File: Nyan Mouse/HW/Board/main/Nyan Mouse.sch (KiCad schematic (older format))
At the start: 11 parts, among them M101 BATTBALANCE-2S, P101 Controller Connector, P102 CONN_4, P103 CONN_2, P104 CONN_2, U101 DRV8837, U102 DRV8837

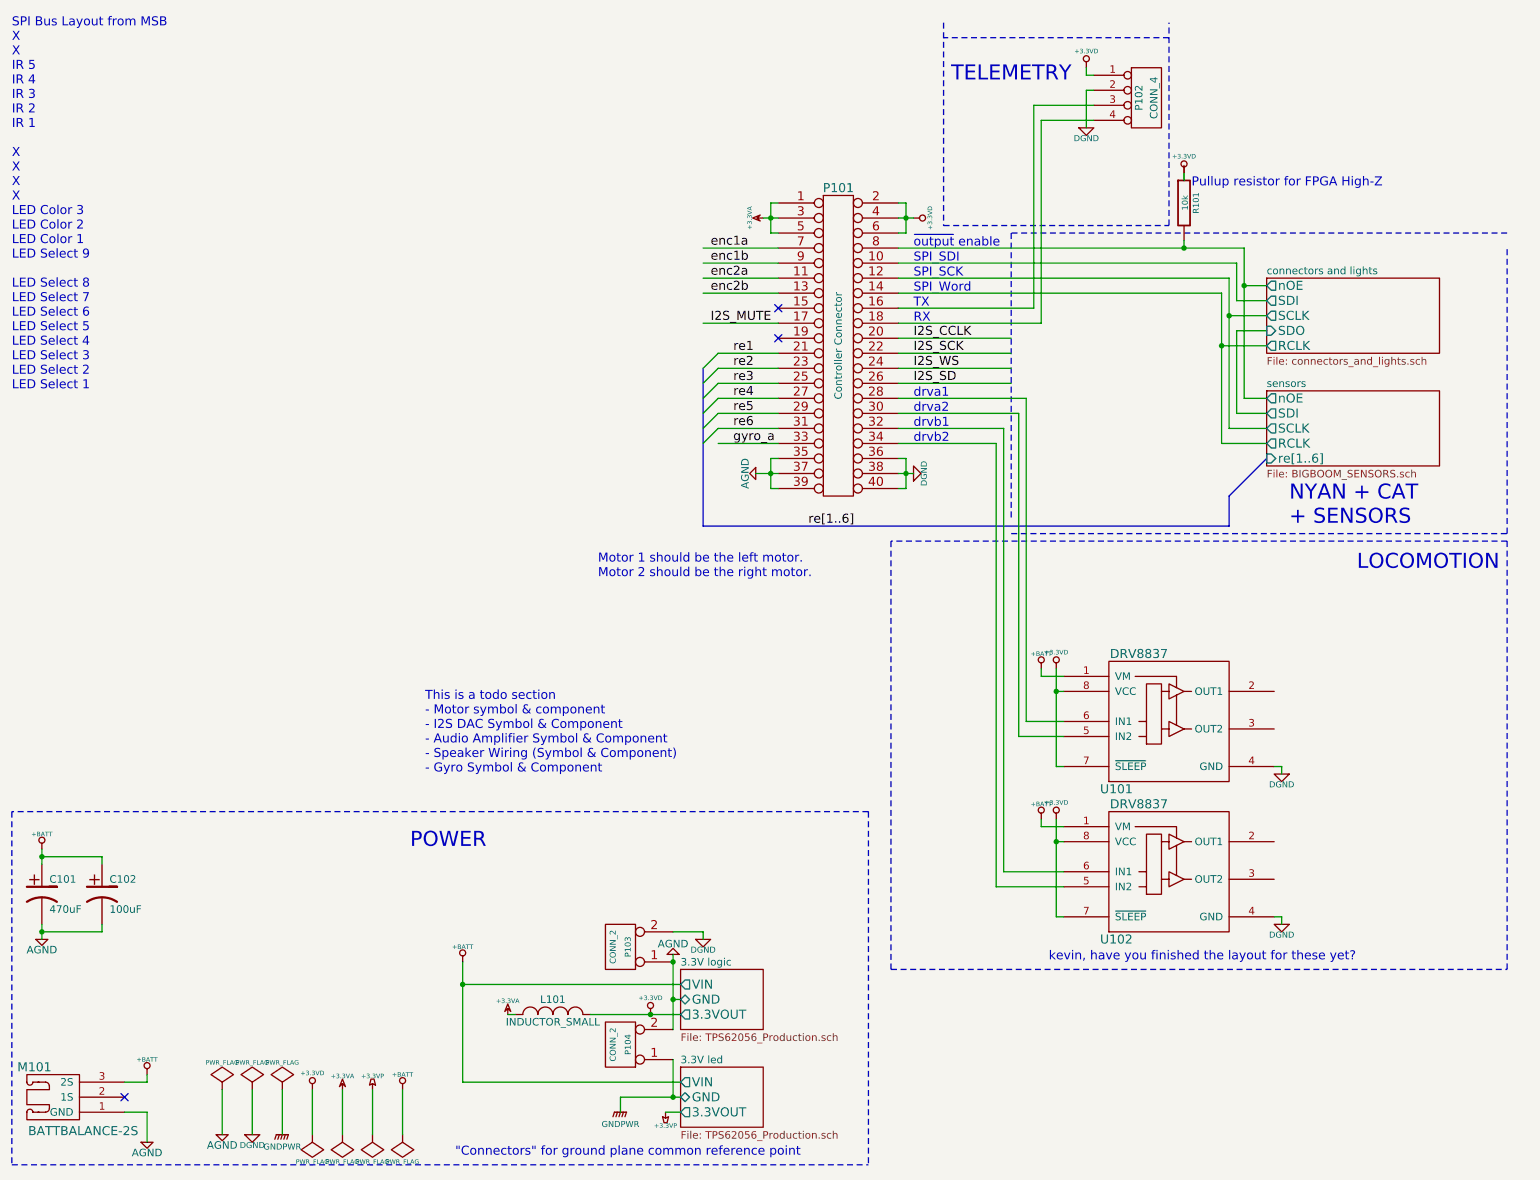
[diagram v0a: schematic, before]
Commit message: Created I2C component (will be changed later because of errors).
Add I2C to board connector on main board (daughter board yet to be done).
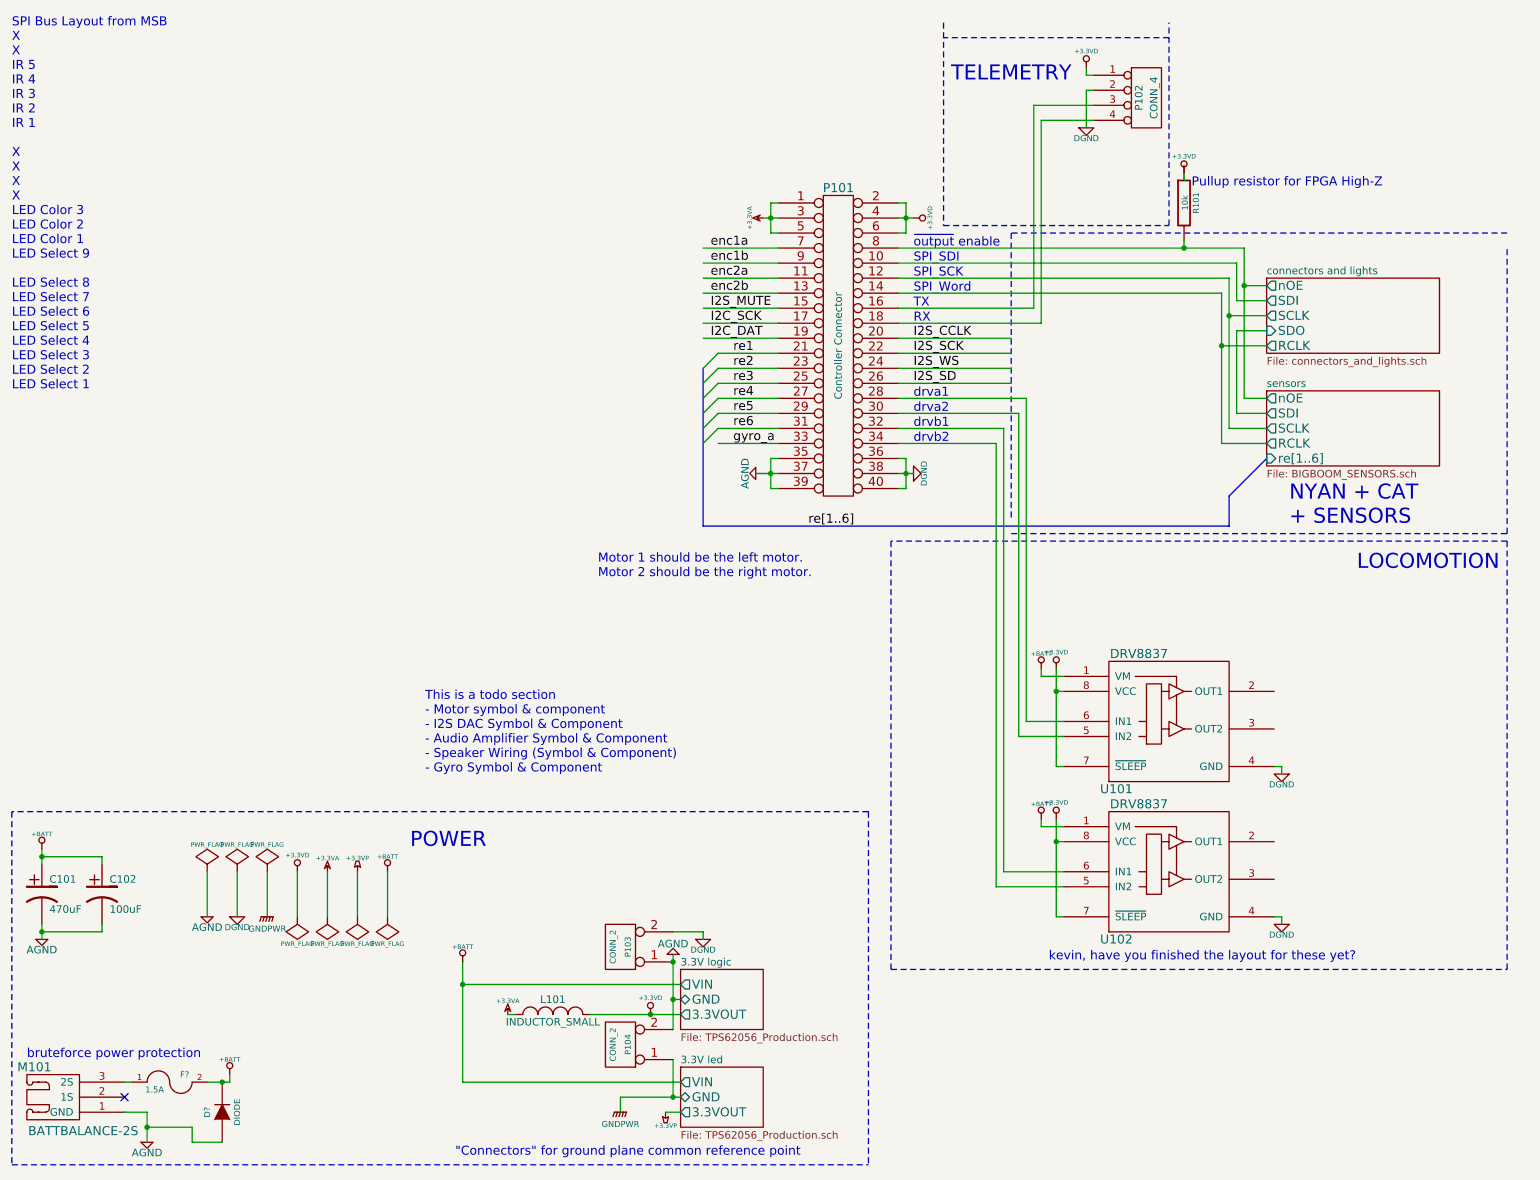
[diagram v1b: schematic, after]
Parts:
- added D?: DIODE, symbol DIODE
- added F?: 1.5A, symbol FUSE
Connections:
- net labels added: I2C_DAT, I2C_SCK
- wire segments 118 -> 124
- no-connect marks 3 -> 1
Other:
- note added: "bruteforce power protection"

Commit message: Updated schematic and added craptons of symbols.
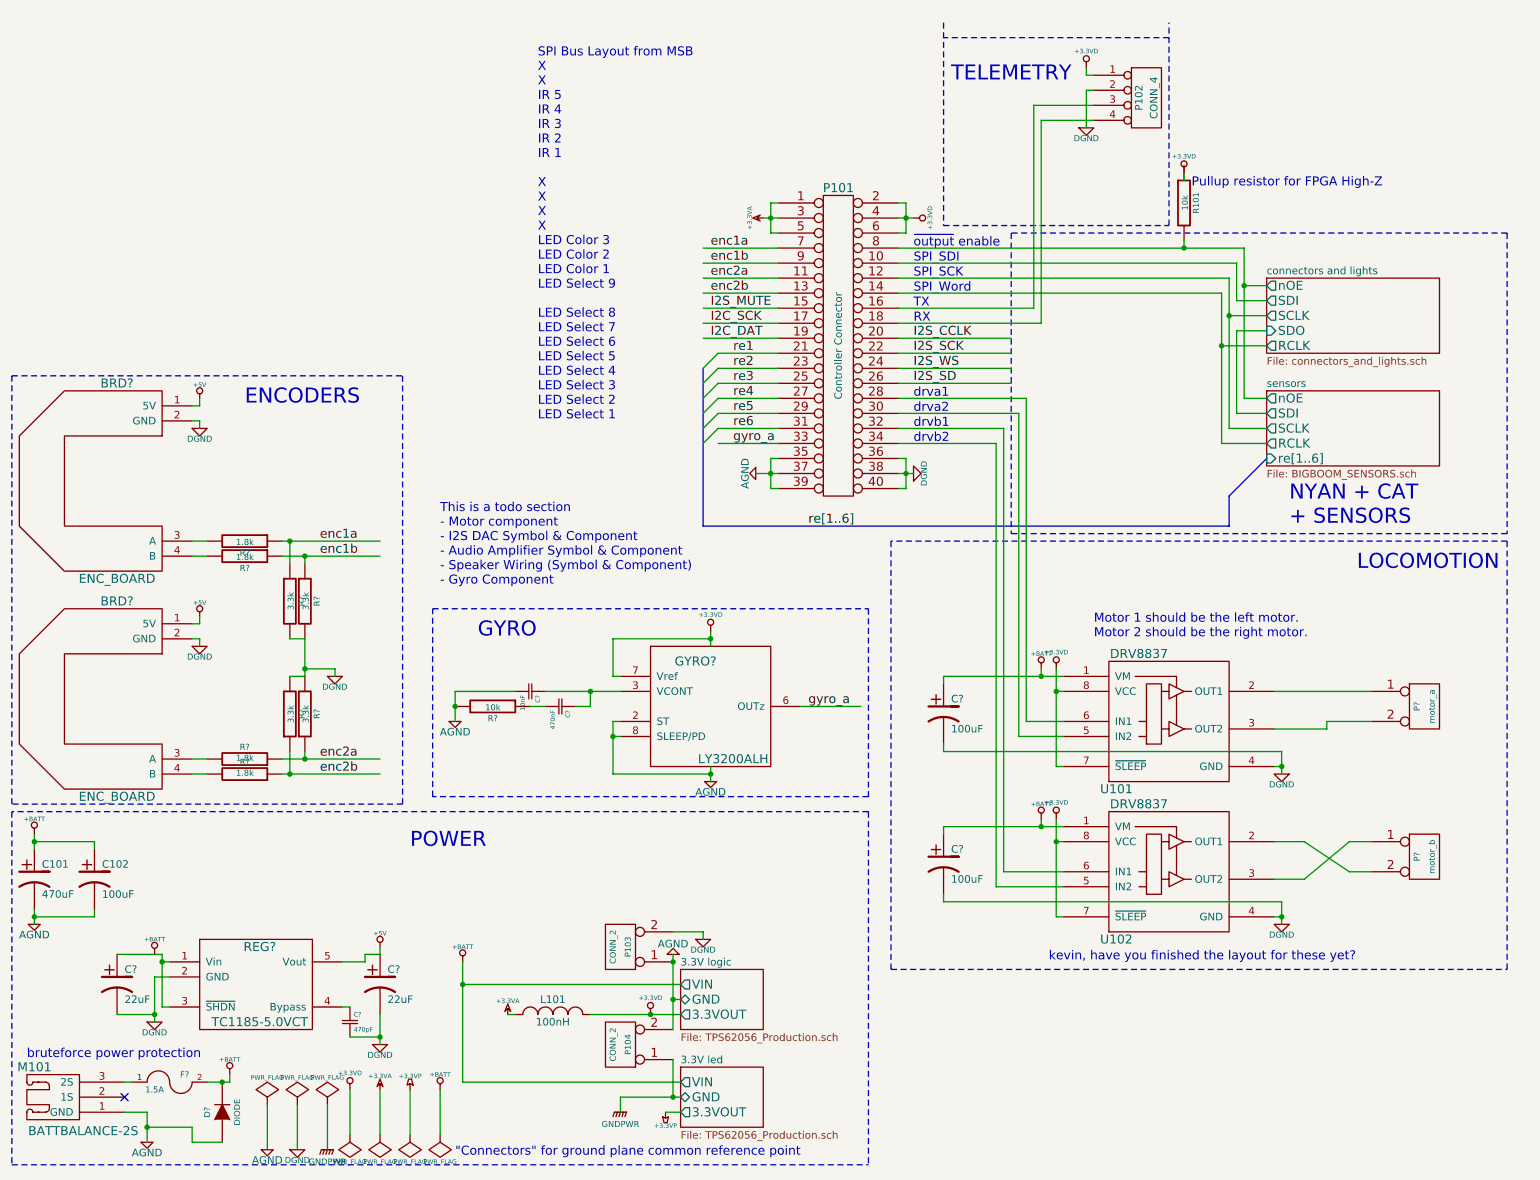
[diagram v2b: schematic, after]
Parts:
- added BRD? (x2): ENC_BOARD, symbol ENC_BOARD
- added C? (x2): 22uF, symbol CP1
- added C?: 470pF, symbol Csmall
- added C? (x2): 100uF, symbol CP1
- added C?: 10nF, symbol Csmall
- added C?: 470nF, symbol Csmall
- added GYRO?: LY3200ALH, symbol LY3200ALH
- added P?: motor_a, symbol CONN_2
- added P?: motor_b, symbol CONN_2
- added R? (x4): 1.8k, symbol R
- added R? (x4): 3.3k, symbol R
- added R?: 10k, symbol R
- added REG?: TC1185-5.0VCT, symbol TC1185-5.0VCT
- L101: value INDUCTOR_SMALL -> 100nH
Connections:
- net labels added: +5V
- wire segments 124 -> 195
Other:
- note added: "ENCODERS"
- note added: "GYRO"
- note added: "This is a todo section\n- Motor component\n- I2S DAC Symbol & Component\n- Audio Amplifier Symbol & Component\n- Speaker Wiring (Symbol & Component)\n- Gyro Component"
- note removed: "This is a todo section\n- Motor symbol & component\n- I2S DAC Symbol & Component\n- Audio Amplifier Symbol & Component\n- Speaker Wiring (Symbol & Component)\n- Gyro Symbol & Component"
- moved on the sheet: C101, C102
